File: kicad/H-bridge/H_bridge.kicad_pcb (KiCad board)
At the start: 2 copper layers, 149.9 x 87.6 mm, 33 parts, among them J1 Screw_Terminal_01x02, J2 Conn_Coaxial, J3 Screw_Terminal_01x02, Q1 Q_NPN_Darlington_BCE, Q2 Q_NMOS_GDS, Q3 Q_NMOS_GDS, U1 LTV-817, U2 PDS1-S15-S15-M

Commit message: First iteration of the layout
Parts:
- removed C8: C, Capacitors_SMD:C_1210
- removed R10: R_US, Resistors_THT:R_Axial_DIN0617_L17.0mm_D6.0mm_P30.48mm_Horizontal
- removed R11: R_US, Resistors_THT:R_Axial_DIN0207_L6.3mm_D2.5mm_P15.24mm_Horizontal
- removed R7: R_US, Resistors_SMD:R_1206
- removed R8, R9: R_US, Resistors_SMD:R_0805
- added D1: PMEG10020AELRX, Diode_SMD:Nexperia_CFP3_SOD-123W, F.Cu at (176.0, 102.0)
- added D2: PMEG10020AELRX, Diode_SMD:Nexperia_CFP3_SOD-123W, F.Cu at (176.0, 104.5)
- added Q4: IAUT300N10S5N014ATMA1, Package_TO_SOT_SMD:Infineon_PG-HSOF-8-1_ThermalVias, F.Cu at (195.3, 116.6)
- added RV1: V20E50P (80V), Varistor:RV_Disc_D15.5mm_W7.5mm_P7.5mm, F.Cu at (188.2, 103.5)
- added U3: HIP4080A, Package_SO:SO-20_12.8x7.5mm_P1.27mm, F.Cu at (168.0, 103.5)
- C1, C2, C3, C5, C6: footprint Capacitors_SMD:C_0805 -> Capacitor_SMD:C_0805_2012Metric
- C4, C9: footprint Capacitors_SMD:C_1210 -> Capacitor_SMD:C_0805_2012Metric
- C7: footprint Capacitors_THT:C_Disc_D7.5mm_W5.0mm_P10.00mm -> Capacitor_SMD:C_0805_2012Metric
- J3: value Screw_Terminal_01x02 -> 2453710000; footprint TerminalBlock:TerminalBlock_Altech_AK300-2_P5.00mm -> footprints:CONN_2453710000; moved to B.Cu
- Q1: value Q_NPN_Darlington_BCE -> IAUT300N10S5N014ATMA1; footprint TO_SOT_Packages_THT:TO-220-3_Vertical -> Package_TO_SOT_SMD:Infineon_PG-HSOF-8-1_ThermalVias
- Q2, Q3: value Q_NMOS_GDS -> IAUT300N10S5N014ATMA1; footprint Coil_speedifier:STE250NS10 -> Package_TO_SOT_SMD:Infineon_PG-HSOF-8-1_ThermalVias
- R1: value R_US -> 220
- R2: value R_US -> 10k; footprint Resistors_SMD:R_1206 -> Resistor_SMD:R_0805_2012Metric
- R3: footprint Resistors_SMD:R_1206 -> Resistor_SMD:R_0805_2012Metric
- R4, R5, R6: footprint Resistors_SMD:R_0805 -> Resistor_SMD:R_0805_2012Metric
- moved C7 50.9 mm to (175.9, 99.5), turned to 0 degrees
- moved R2 45.3 mm to (134.5, 107.1)
- moved C6 39.0 mm to (140.3, 122.4)
- moved L4 39.0 mm to (137.2, 121.4)
- moved L5 39.0 mm to (137.2, 124.0)
- moved U2 39.0 mm to (126.3, 121.7)
- moved C1 39.0 mm to (122.0, 137.4)
- moved C2 39.0 mm to (121.8, 131.6)
- moved L3 39.0 mm to (125.1, 129.9)
- moved R1 39.0 mm to (119.5, 100.8)
- moved U1 39.0 mm to (124.0, 100.8)
- moved C5 39.0 mm to (134.5, 122.4)
- moved L1 39.0 mm to (120.7, 134.4)
- moved L2 39.0 mm to (123.0, 134.4)
- moved J3 31.7 mm to (210.0, 125.3)
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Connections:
- C3 pad 1: Net-(C3-Pad1) -> Net-(D2-K)
- C3 pad 2: GNDD -> Coil_B
- C4 pad 1: Net-(C4-Pad1) -> Net-(U3-IN-)
- C7 pad 1: Net-(C7-Pad1) -> Net-(D1-K)
- C7 pad 2: Net-(C7-Pad2) -> Coil_A
- C9 pad 1: Net-(C4-Pad1) -> +15V
- J3 pad 1: Net-(C7-Pad1) -> Current_in
- J3 pad 2: Net-(J3-Pad2) -> Coil_A
- Q1 pad 1: Net-(Q1-Pad1) -> Current_in
- Q1 pad 3: GNDD -> Coil_A
- Q2 pad 1: Net-(Q2-Pad1) -> Coil_A
- Q2 pad 2: Net-(C7-Pad1) -> Net-(Q2-G)
- Q3 pad 1: Net-(Q3-Pad1) -> Current_in
- Q3 pad 2: Net-(J3-Pad2) -> Net-(Q3-G)
- Q3 pad 3: GNDD -> Coil_B
- R2 pad 1: +15V -> Net-(U3-IN+)
- R2 pad 2: Net-(C3-Pad1) -> GNDD
- R3 pad 1: Net-(C3-Pad1) -> Net-(U3-HDEL)
- R4 pad 1: Net-(R4-Pad1) -> Net-(U3-LDEL)
- R4 pad 2: Net-(Q1-Pad1) -> GNDD
- R5 pad 1: Net-(Q1-Pad1) -> +15V
- R5 pad 2: GNDD -> Net-(U3-IN-)
- R6 pad 1: +15V -> Net-(U3-IN-)
- R6 pad 2: Net-(C4-Pad1) -> GNDD
- U1 pad 3: Net-(R4-Pad1) -> Net-(U3-IN+)
- U1 pad 4: Net-(C3-Pad1) -> +15V
- U2 pad 14: Net-(U2-Pad14) -> unconnected-(U2-NC-Pad14)
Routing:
- net Net-(J3-Pad2): track 240.5 -> 0.00 mm
- net Net-(C7-Pad1): track 140.1 -> 0.00 mm
- net Net-(J1-Pin_1): track 66.0 -> 24.4 mm, vias 1 -> 0
- net Net-(J2-In): track 46.4 -> 7.36 mm, vias 1 -> 0
- net Net-(Q3-G): track 0.00 -> 35.0 mm, vias 0 -> 2
- net Coil_A: track 0.00 -> 31.3 mm, vias 0 -> 1
- net Net-(Q3-Pad1): track 30.8 -> 0.00 mm
- net Net-(Q2-Pad1): track 30.4 -> 0.00 mm
- net Net-(Q4-G): track 0.00 -> 29.4 mm, vias 0 -> 2
- net Net-(C3-Pad1): track 24.8 -> 0.00 mm
- net Net-(Q2-G): track 0.00 -> 23.1 mm, vias 0 -> 2
- net Net-(D2-K): track 0.00 -> 18.3 mm
- net Net-(Q1-Pad1): track 18.2 -> 0.00 mm
- net Net-(D1-K): track 0.00 -> 17.6 mm
- net GNDD: track 110.7 -> 126.6 mm, vias 0 -> 3
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- added copper zone on B.Cu, net Coil_A
- added copper zone on F.Cu, net Coil_A
- added copper zone on B.Cu, net Coil_B
- added copper zone on F.Cu, net Coil_B
- added copper zone on B.Cu, net Current_in
- added copper zone on F.Cu, net Current_in
- added copper zone on B.Cu, net GNDD
- added copper zone on F.Cu, net GNDD
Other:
- outline, holes or cut-outs redrawn

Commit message: 2nd iteration
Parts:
- added H1: MountingHole, MountingHole:MountingHole_3.5mm, F.Cu at (273.1, 21.3)
- added H2: MountingHole, MountingHole:MountingHole_3.5mm, F.Cu at (273.1, 29.9)
- added H3: MountingHole, MountingHole:MountingHole_3.5mm, F.Cu at (273.1, 38.4)
- added H4: MountingHole, MountingHole:MountingHole_3.5mm, F.Cu at (273.1, 47.0)
- moved C3 37.2 mm to (139.2, 107.6), turned to -90 degrees
- moved D2 37.1 mm to (139.2, 99.2), turned to 90 degrees
- moved Q1 30.9 mm to (165.3, 119.0)
- moved Q3 25.7 mm to (187.9, 119.0)
- moved Q2 24.4 mm to (165.4, 101.2), turned to 90 degrees
- moved D1 23.6 mm to (152.6, 99.2), turned to 90 degrees
- moved U3 21.6 mm to (146.9, 108.0), turned to -90 degrees
- moved C7 21.1 mm to (155.1, 103.2), turned to -90 degrees
- moved R4 21.1 mm to (141.6, 99.6), turned to 90 degrees
- moved C9 20.9 mm to (146.9, 115.6)
- moved R3 16.9 mm to (143.6, 100.1), turned to 90 degrees
- moved Q4 16.4 mm to (187.6, 102.1), turned to 90 degrees
- moved C4 15.0 mm to (146.4, 100.9), turned to 0 degrees
- moved RV1 14.1 mm to (174.8, 107.8), turned to 90 degrees
- moved R6 13.8 mm to (146.4, 98.9), turned to 0 degrees
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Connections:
- Q1 pad 1: Current_in -> Net-(Q1-D)
- Q1 pad 2: Net-(Q1-G) -> Current_in
- Q2 pad 1: Coil_A -> Net-(Q2-D)
- Q2 pad 2: Net-(Q2-G) -> Coil_A
- Q3 pad 1: Current_in -> Net-(Q3-G)
- Q3 pad 2: Net-(Q3-G) -> Current_in
- Q4 pad 1: Coil_B -> Net-(Q4-D)
- Q4 pad 2: Net-(Q4-G) -> Coil_B
- U3 pad 13: Net-(Q4-G) -> Net-(Q4-D)
- U3 pad 18: Net-(Q2-G) -> Net-(Q2-D)
- U3 pad 20: Net-(Q1-G) -> Net-(Q1-D)
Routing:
- net GNDD: track 126.6 -> 17.7 mm, vias 3 -> 7
- net Coil_B: track 3.17 -> 57.7 mm, vias 0 -> 1
- net Net-(Q4-D): track 0.00 -> 48.4 mm
- net Net-(Q4-G): track 29.4 -> 0.00 mm, vias 2 -> 0
- net +15V: track 16.7 -> 45.5 mm, vias 0 -> 2
- net Net-(Q2-G): track 23.1 -> 0.00 mm, vias 2 -> 0
- net Net-(Q3-G): track 35.0 -> 51.3 mm
- net Coil_A: track 31.3 -> 15.2 mm, vias 1 -> 2
- net Net-(Q1-D): track 0.00 -> 15.7 mm
- net Net-(Q2-D): track 0.00 -> 15.6 mm
- net Net-(Q1-G): track 14.5 -> 0.00 mm, vias 2 -> 0
- net Net-(D1-K): track 17.6 -> 7.52 mm
- net Net-(D2-K): track 18.3 -> 9.73 mm
- net Net-(J2-In): track 7.36 -> 4.45 mm
- net Net-(U3-HDEL): track 4.89 -> 2.22 mm
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- removed copper zone on B.Cu, net Coil_B
- removed copper zone on B.Cu, net Current_in
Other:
- board size 149.9 x 87.6 mm -> 127 x 76.2 mm

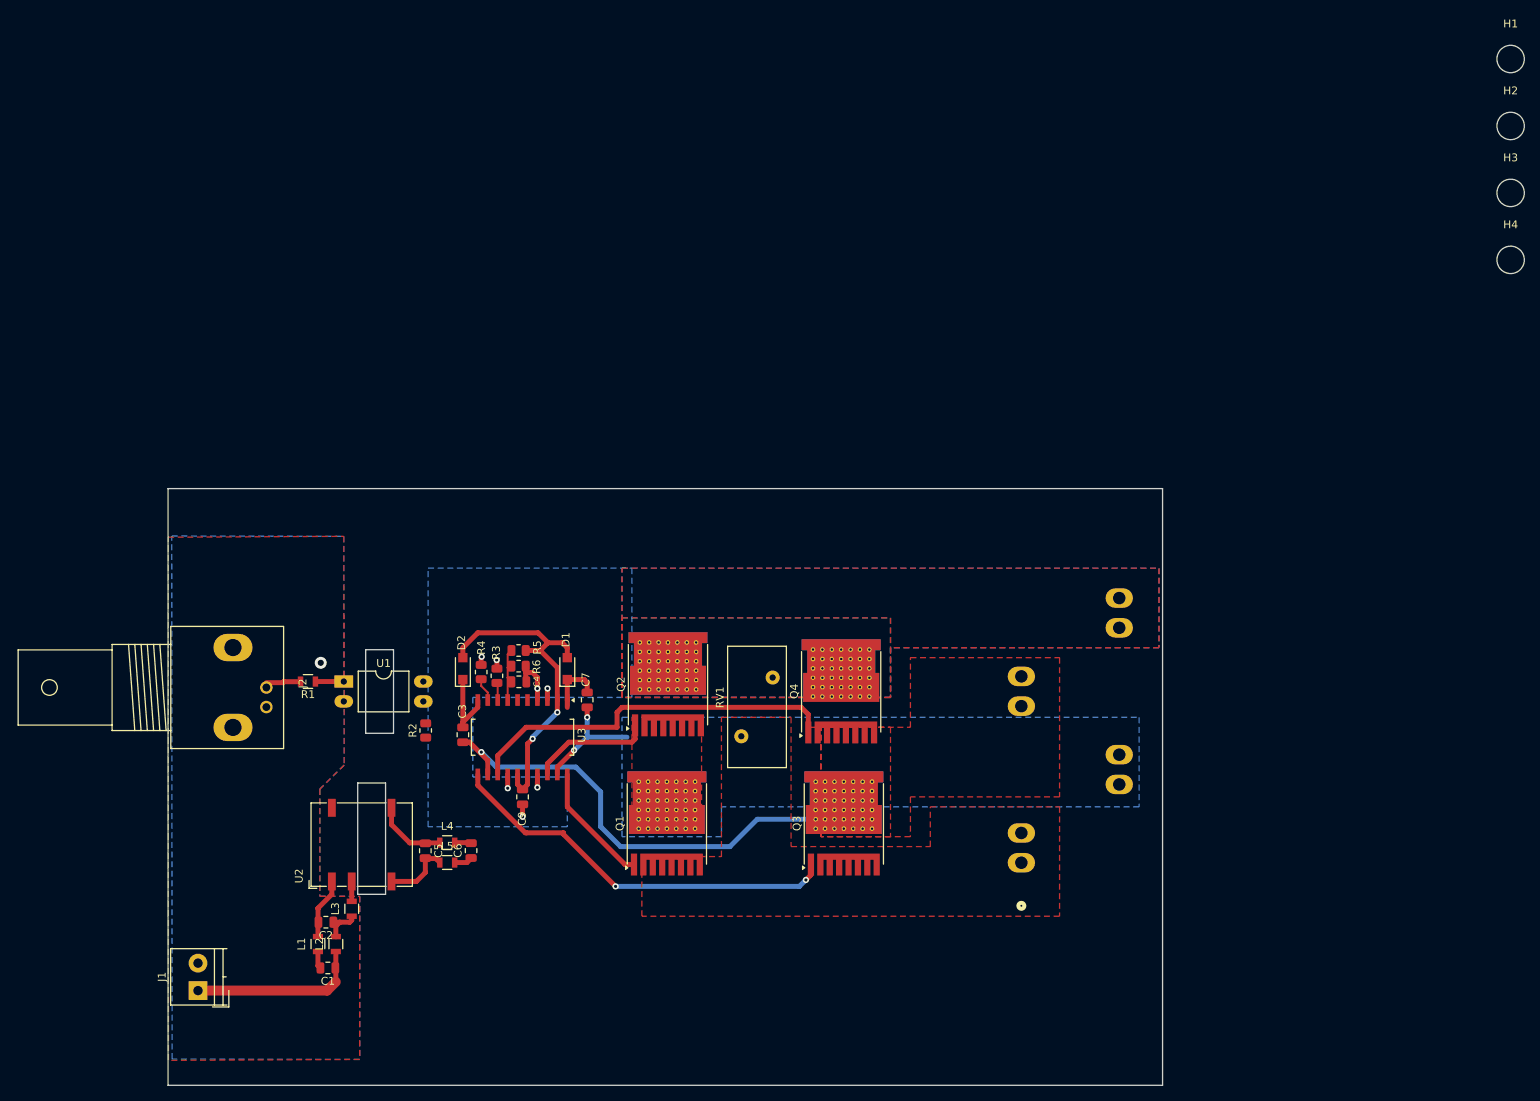
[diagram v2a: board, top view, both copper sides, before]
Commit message: H_bridge circuit with current control ciruit added
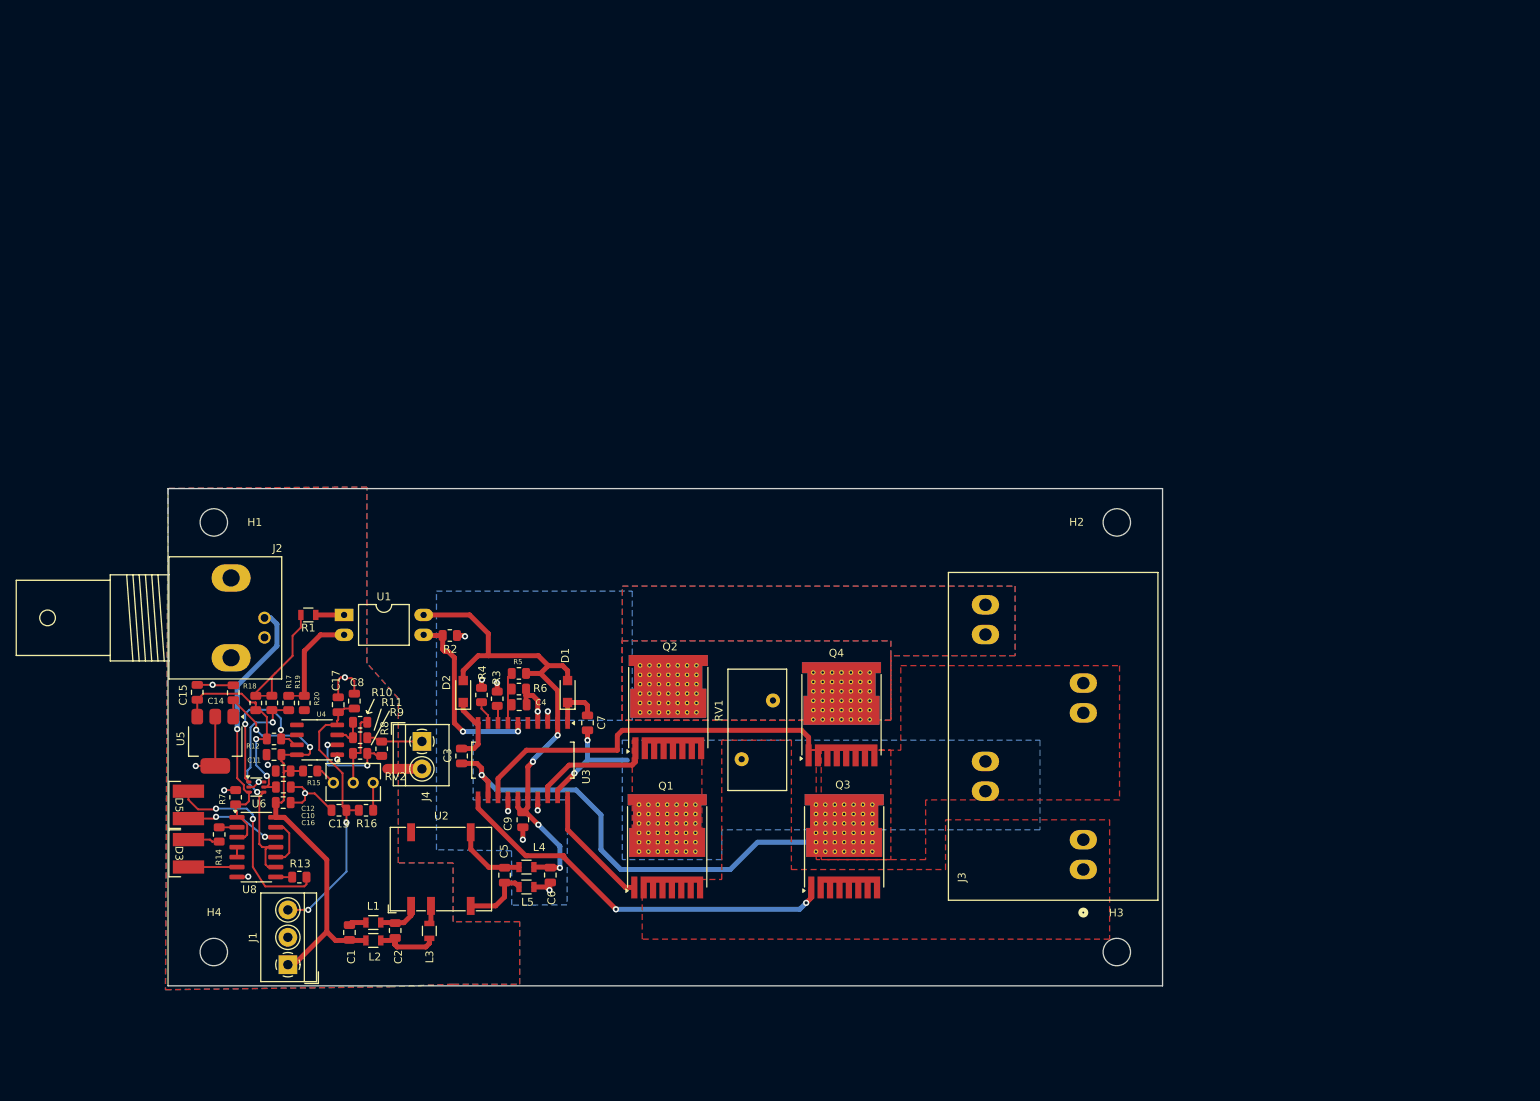
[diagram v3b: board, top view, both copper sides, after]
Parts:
- added C10: C, Capacitor_SMD:C_0805_2012Metric, F.Cu at (116.3, 114.3)
- added C11: C, Capacitor_SMD:C_0805_2012Metric, F.Cu at (115.1, 110.2)
- added C12: C, Capacitor_SMD:C_0805_2012Metric, F.Cu at (116.3, 112.3)
- added C13: C, Capacitor_SMD:C_0805_2012Metric, F.Cu at (123.4, 117.3)
- added C14: C, Capacitor_SMD:C_0805_2012Metric, F.Cu at (109.9, 102.3)
- added C15: C, Capacitor_SMD:C_0805_2012Metric, F.Cu at (105.3, 102.2)
- added C16: C, Capacitor_SMD:C_0805_2012Metric, F.Cu at (116.3, 116.3)
- added C17: C, Capacitor_SMD:C_0805_2012Metric, F.Cu at (123.3, 103.8)
- added C8: C, Capacitor_SMD:C_0805_2012Metric, F.Cu at (125.4, 103.3)
- added D3: AA4040R3G2CT/R-10MAT, footprints:LED_boomerang, F.Cu at (104.2, 122.8)
- added D5: AA4040R3G2CT/R-10MAT, footprints:LED_boomerang, F.Cu at (104.2, 116.6)
- added J4: Screw_Terminal_01x02, TerminalBlock_4Ucon:TerminalBlock_4Ucon_1x02_P3.50mm_Horizontal, F.Cu at (134.0, 108.5)
- added R10: R_US, Resistor_SMD:R_0805_2012Metric, F.Cu at (126.1, 106.0)
- added R11: R_US, Resistor_SMD:R_0805_2012Metric, F.Cu at (126.1, 108.0)
- added R12: R_US, Resistor_SMD:R_0805_2012Metric, F.Cu at (115.1, 108.2)
- added R13: R_US, Resistor_SMD:R_0805_2012Metric, F.Cu at (118.4, 125.8)
- added R14: R_US, Resistor_SMD:R_0805_2012Metric, F.Cu at (108.1, 120.4)
- added R15: 0, Resistor_SMD:R_0805_2012Metric, F.Cu at (119.7, 112.3)
- added R16: 0, Resistor_SMD:R_0805_2012Metric, F.Cu at (126.9, 117.3)
- added R17: 0, Resistor_SMD:R_0805_2012Metric, F.Cu at (114.9, 103.6)
- added R18: DNP, Resistor_SMD:R_0805_2012Metric, F.Cu at (112.8, 103.6)
- added R19: DNP, Resistor_SMD:R_0805_2012Metric, F.Cu at (117.0, 103.6)
- added R20: 0, Resistor_SMD:R_0805_2012Metric, F.Cu at (119.0, 103.6)
- added R7: R_US, Resistor_SMD:R_0805_2012Metric, F.Cu at (110.2, 115.6)
- added R8: 0, Resistor_SMD:R_0805_2012Metric, F.Cu at (128.9, 109.4)
- added R9: DNP, Resistor_SMD:R_0805_2012Metric, F.Cu at (126.1, 110.0)
- added RV2: 100k, Potentiometer_THT:Potentiometer_Bourns_3266Y_Vertical, F.Cu at (122.7, 113.8)
- added U4: LT1011, Package_SO:SO-8_3.9x4.9mm_P1.27mm, F.Cu at (120.6, 108.3)
- added U5: LM340MPX-5.0/NOPB, Package_TO_SOT_SMD:SOT-223-3_TabPin2, F.Cu at (107.6, 108.5)
- added U6: 74LVC1G373, Package_TO_SOT_SMD:SOT-363_SC-70-6, F.Cu at (112.9, 114.3)
- added U8: 74AC14DR, Package_SO:SOIC-14_3.9x8.7mm_P1.27mm, F.Cu at (112.9, 122.0)
- J1: value Screw_Terminal_01x02 -> Screw_Terminal_01x03; footprint TerminalBlock_4UCON:TerminalBlock_4UCON_19963_02x3.5mm_Straight -> TerminalBlock_4Ucon:TerminalBlock_4Ucon_1x03_P3.50mm_Horizontal
- J3: moved to F.Cu
- moved H4 187.7 mm to (107.4, 135.4)
- moved H1 175.9 mm to (107.4, 80.5)
- moved H3 109.2 mm to (222.8, 135.4)
- moved H2 71.4 mm to (222.8, 80.5)
- moved R2 12.5 mm to (137.6, 95.0), turned to 0 degrees
- moved J1 11.9 mm to (116.9, 137.0)
- moved C6 10.6 mm to (150.4, 125.6)
- moved L4 10.6 mm to (147.4, 124.5)
- moved L5 10.6 mm to (147.4, 127.1)
- moved U2 10.6 mm to (136.4, 124.8)
- moved C5 10.6 mm to (144.6, 125.6)
- moved L3 10.3 mm to (135.0, 132.7)
- moved C2 8.91 mm to (130.6, 132.6), turned to 90 degrees
- moved J2 8.89 mm to (108.9, 92.7)
- moved R1 8.50 mm to (119.5, 92.3)
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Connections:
- net Net-(J1-Pin_1) renamed VCC
- J2 pad 1: Net-(J2-In) -> /protection/input
- R1 pad 2: Net-(J2-In) -> /protection/output +
- U1 pad 2: GND -> /protection/output -
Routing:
- net GND: track 2.24 -> 41.5 mm, vias 1 -> 9
- net VCC: track 22.0 -> 61.1 mm, vias 0 -> 2
- net VEE: track 0.00 -> 37.1 mm, vias 0 -> 2
- net /protection/input: track 0.00 -> 36.1 mm, vias 0 -> 1
- net Net-(U6-Q): track 0.00 -> 30.6 mm, vias 0 -> 2
- net +5V: track 0.00 -> 26.1 mm, vias 0 -> 2
- net Net-(D5-KA): track 0.00 -> 26.1 mm, vias 0 -> 2
- net Net-(U3-IN+): track 0.00 -> 24.2 mm, vias 0 -> 2
- net +15V: track 45.5 -> 68.1 mm, vias 2 -> 4
- net Net-(U6-LE): track 0.00 -> 19.1 mm, vias 0 -> 2
- net /protection/output +: track 0.00 -> 17.9 mm
- net /protection/output -: track 0.00 -> 13.7 mm
- net Net-(U4-+): track 0.00 -> 12.6 mm, vias 0 -> 2
- net Net-(D5-AK): track 0.00 -> 12.2 mm, vias 0 -> 2
- net Net-(R10-Pad1): track 0.00 -> 9.46 mm
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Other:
- board size 127 x 76.2 mm -> 127 x 63.5 mm

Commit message: Fixed silkscreen placement
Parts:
- moved C7 0.57 mm to (154.7, 106.5)
- moved R4 0.48 mm to (141.6, 103.0)
- moved R13 0.19 mm to (118.4, 125.6)
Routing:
- net GNDD: track 19.5 -> 22.2 mm
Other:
- board text added: "I accidentaly deleted the refrence label for J3. I added it back but I don't know if it is connected properly"
- board text added: "The margins of C14, C15 and J2 are touching"
- board text added: "j3"

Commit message: Added C18, logo and other footprints
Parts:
- added C18: 100nF, Capacitor_SMD:C_0805_2012Metric, F.Cu at (127.5, 101.5)
- added LOGO_1: ~, footprints:JQI-Logo, F.Cu at (150.5, 87.0)
- C1, C2, C6, C8: value C -> 22uF
- C10, C11, C12, C13, C14, C15, C16, C17, C4, C9: value C -> 100nF
- C3, C7: value C -> 47nF
- C5: value C -> DNP
- L1, L2, L3, L4, L5: value INDUCTOR -> 4.7k
- R10: value R_US -> DNP
- R11: value R_US -> 0
- R12, R5, R6, R7: value R_US -> 10k
- R13, R14: value R_US -> 330
- R3, R4: value R_US -> 100k
- R8: value 0 -> DNP
- R9: value DNP -> 0
- moved C15 0.84 mm to (105.0, 103.0), turned to 180 degrees
- moved C14 0.73 mm to (109.9, 103.0), turned to 0 degrees
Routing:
- net GND: track 41.5 -> 34.0 mm
- net +5V: track 26.1 -> 30.3 mm
- net Net-(C18-Pad2): track 9.46 -> 13.2 mm
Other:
- board text added: "+15V"
- board text added: "-15V"
- board text added: "COILB"
- board text added: "CURRENTIN"
- board text added: "GNDD"
- board text removed: "I accidentaly deleted the refrence label for J3. I added it back but I don't know if it is connected properly"
- board text removed: "The margins of C14, C15 and J2 are touching"
- board text removed: "j3"
